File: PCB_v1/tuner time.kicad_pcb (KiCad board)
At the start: 4 copper layers, 80 x 40 mm, 118 parts, among them J1 B6B-PH-K-S, J10 1051640001, J2 B6B-PH-K-S, J3 JST_B2B-XH-A, J4 Conn_01x05_Pin, J5 Conn_01x05_Pin, J6 OLED Conn_02x04, J7 B4B-XH-A, J8 Conn_ARM_JTAG_SWD_10, J9 Conn_01x03, SW1 SW_SPST, SW2 SW_Push, SW3 SW_Push, SW4 SW_Push, SW5 SW_Push, SW6 SW_Push, SW7 SW_Push, SW8 SW_Push, SW9 SW_SPDT, U1 BQ25185DLHR, U2 BQ27441-G1, U3 SMS05T1G, U4 SMS05T1G, U5 DRV8834PWP, U6 STM32F405RGTx, U7 ESD9B5.0ST5G, Y1 Crystal

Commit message: before major move
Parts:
- removed the C15 at (181.3, 114.4)
- removed the C18 at (183.7, 120.7)
- removed the C19 at (181.2, 114.2)
- removed the C20 at (181.4, 116.2)
- removed C29: 100nF, C_0805_2012Metric
- removed C30: 1uF, C_1206_3216Metric_Pad1.33x1.80mm_HandSolder
- removed FB1: FerriteBead, L_0603_1608Metric
- removed JP3: M2, SolderJumper-3_P1.3mm_Open_RoundedPad1.0x1.5mm
- removed JP4: SLP, SolderJumper-3_P1.3mm_Bridged12_RoundedPad1.0x1.5mm
- removed the R21 at (180.9, 119.9)
- removed RN4: 22, RESCAXE80P320X160X70-8N
- removed TP1, TP2: ~, TestPoint_THTPad_D1.0mm_Drill0.5mm
- removed the TP8 at (184.4, 116.2)
- removed XTAL1: MC-306 32.7680K-E3:ROHS, SO4_MC-306_SEC
- removed Y1: Crystal, LFXTAL003237Bulk
- added H3: MountingHole, MountingHole:MountingHole_2.2mm_M2_DIN965_Pad_TopOnly, F.Cu at (152.7, 137.3)
- added J9: Conn_02x05_Odd_Even, Connector_IDC:IDC-Header_2x05_P2.54mm_Vertical, F.Cu at (196.3, 104.2)
- added JP5: M1, Jumper:SolderJumper-3_P1.3mm_Open_RoundedPad1.0x1.5mm, F.Cu at (239.4, 102.0)
- added JP6: M2, Jumper:SolderJumper-3_P1.3mm_Open_RoundedPad1.0x1.5mm, F.Cu at (239.4, 105.9)
- added JP7: SLP, Jumper:SolderJumper-3_P1.3mm_Bridged12_RoundedPad1.0x1.5mm, F.Cu at (239.4, 109.7)
- added R23: 10k, Resistor_SMD:R_0805_2012Metric, F.Cu at (178.5, 117.8)
- added R24: 47k, Resistor_SMD:R_0805_2012Metric, F.Cu at (244.4, 104.7)
- added TP13: ~, Library:TestPoint_THTPad_D0.8mm_Drill0.4mm, F.Cu at (243.2, 110.3)
- added U6: MAX7375AXR805, Package_TO_SOT_SMD:SOT-323_SC-70, F.Cu at (160.4, 80.3)
- C1, C11, C12, C13, C14, C2, C3, C4, C5, C8, C9: footprint C_0805_2012Metric -> Capacitor_SMD:C_0805_2012Metric
- C15: renamed from C17; footprint C_0805_2012Metric -> Capacitor_SMD:C_0805_2012Metric
- C16: value 0.01uF -> 100nF; footprint C_0805_2012Metric -> Capacitor_SMD:C_0805_2012Metric
- C17: renamed from C21; footprint C_0805_2012Metric -> Capacitor_SMD:C_0805_2012Metric
- C18: renamed from C22; footprint C_0805_2012Metric -> Capacitor_SMD:C_0805_2012Metric
- C19: renamed from C23; footprint C_0805_2012Metric -> Capacitor_SMD:C_0805_2012Metric
- C20: renamed from C24; footprint C_0805_2012Metric -> Capacitor_SMD:C_0805_2012Metric
- C21: renamed from C25; footprint C_0805_2012Metric -> Capacitor_SMD:C_0805_2012Metric
- C22: renamed from C26; footprint C_0805_2012Metric -> Capacitor_SMD:C_0805_2012Metric
- C23: renamed from C27; footprint C_0805_2012Metric -> Capacitor_SMD:C_0805_2012Metric
- C24: renamed from C28; footprint C_0805_2012Metric -> Capacitor_SMD:C_0805_2012Metric
- C25: renamed from C31; footprint C_1206_3216Metric_Pad1.33x1.80mm_HandSolder -> Capacitor_SMD:C_1206_3216Metric_Pad1.33x1.80mm_HandSolder
- D3: footprint LED_0805_2012Metric_Pad1.15x1.40mm_HandSolder -> LED_SMD:LED_0805_2012Metric_Pad1.15x1.40mm_HandSolder
- H1, H2: footprint MountingHole_2.2mm_M2_DIN965_Pad_TopOnly -> MountingHole:MountingHole_2.2mm_M2_DIN965_Pad_TopOnly
- J10: renamed from J9; footprint PinHeader_1x03_P2.54mm_Vertical -> Connector_PinHeader_2.54mm:PinHeader_1x03_P2.54mm_Vertical
- J3: value JST_B2B-XH-A -> JST_B2B-PH-K-S; footprint JST_B2B-XH-A -> GT_library:JST_B2B-PH-K-S
- J4, J5: footprint PinHeader_1x05_P2.54mm_Vertical -> Connector_PinHeader_2.54mm:PinHeader_1x05_P2.54mm_Vertical
- J6: footprint PinHeader_2x04_P2.54mm_Vertical -> Connector_PinHeader_2.54mm:PinHeader_2x04_P2.54mm_Vertical
- J8: value Conn_ARM_JTAG_SWD_10 -> Conn_01x02_Pin; footprint PinHeader_2x05_P2.54mm_Vertical -> Connector_PinHeader_2.54mm:PinHeader_1x02_P2.54mm_Vertical
- JP1: footprint SolderJumper-2_P1.3mm_Bridged2Bar_RoundedPad1.0x1.5mm -> Jumper:SolderJumper-2_P1.3mm_Bridged2Bar_RoundedPad1.0x1.5mm
- JP2: value M1 -> SolderJumper_2_Open; footprint SolderJumper-3_P1.3mm_Open_RoundedPad1.0x1.5mm -> Jumper:SolderJumper-2_P1.3mm_Open_RoundedPad1.0x1.5mm; moved to F.Cu
- R1, R10, R11, R12, R13, R14, R15, R16, R17, R18, R19, R2, R20, R3, R4, R5, R6, R7, R8, R9: footprint R_0805_2012Metric -> Resistor_SMD:R_0805_2012Metric
- R21: renamed from R22; footprint R_0805_2012Metric -> Resistor_SMD:R_0805_2012Metric
- R22: renamed from R23; footprint R_0805_2012Metric -> Resistor_SMD:R_0805_2012Metric
- RN1, RN2: footprint RESCAXE50P280X160X55-16N -> Parts_Library:RESCAXE50P280X160X55-16N
- RN3: footprint RESCAXS80P320X160X60-8N -> Parts_Library:RESCAXS80P320X160X60-8N
- RV1: footprint TRIM_TC33X-2-103E -> Parts_Library:TRIM_TC33X-2-103E
- SW9: footprint SW_SPDT_PCM12 -> Button_Switch_SMD:SW_SPDT_PCM12
- TP10: renamed from TP11; footprint TestPoint_THTPad_D1.0mm_Drill0.5mm -> Library:TestPoint_THTPad_D0.8mm_Drill0.4mm
- TP11: renamed from TP12; footprint TestPoint_THTPad_D1.0mm_Drill0.5mm -> Library:TestPoint_THTPad_D0.8mm_Drill0.4mm
- TP12: renamed from TP13; footprint TestPoint_THTPad_D1.0mm_Drill0.5mm -> Library:TestPoint_THTPad_D0.8mm_Drill0.4mm
- TP3, TP4, TP5, TP6, TP7: footprint TestPoint_THTPad_D1.0mm_Drill0.5mm -> Library:TestPoint_THTPad_D0.8mm_Drill0.4mm
- TP8: renamed from TP9; footprint TestPoint_THTPad_D1.0mm_Drill0.5mm -> Library:TestPoint_THTPad_D0.8mm_Drill0.4mm
- TP9: renamed from TP10; footprint TestPoint_THTPad_D1.0mm_Drill0.5mm -> Library:TestPoint_THTPad_D0.8mm_Drill0.4mm
- U8: renamed from U7; footprint SODFL1006X40N -> Library:SODFL1006X40N
- moved C21 51.2 mm to (244.5, 146.7)
- moved R22 51.2 mm to (242.1, 146.7)
- moved J4 50.3 mm to (217.0, 105.1)
- moved R3 42.4 mm to (244.4, 101.7), turned to 0 degrees
- moved SW9 40.1 mm to (163.1, 74.3), turned to 0 degrees
- moved C16 39.8 mm to (164.8, 79.8), turned to 0 degrees
- moved TP7 38.8 mm to (168.1, 79.3)
- moved C14 38.7 mm to (246.7, 112.8)
- moved R20 38.7 mm to (250.2, 112.8)
- moved JP1 38.7 mm to (245.1, 113.5)
- moved D3 38.6 mm to (244.6, 107.7), turned to 0 degrees
- moved SW8 38.5 mm to (241.7, 141.1)
- moved R18 38.5 mm to (251.9, 139.2)
- moved R19 38.5 mm to (249.9, 139.2)
- moved D6 32.8 mm to (233.7, 93.7)
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- renumbered J10 to J11, U6 to U7
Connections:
- C9 pad 1: 3V3 -> VINT
- J6 pad 5: RST -> MOSI
- J6 pad 8: MOSI -> RST
- JP2 pad 2: /Motor/M1 -> Net-(JP2-B)
- R13 pad 1: 3V3 -> VINT
- R13 pad 2: Net-(U5-CONFIG) -> Net-(JP2-B)
- R17 pad 2: /Motor/SLP -> /Motor/SLEEP
- R3 pad 2: GND -> AGND
- SW9 pad 1: 3V3 -> GND
- SW9 pad 3: GND -> 3V3
- TP7 pad 1: PC14-OSC32IN -> PH1-OSCOUT
- U5 pad 1: /Motor/A1 -> /Motor/SLEEP
- U5 pad 10: /Motor/M0 -> /Motor/EN
- U5 pad 11: /Motor/M1 -> STEP
- U5 pad 12: Net-(U5-CONFIG) -> DIR
- U5 pad 13: Net-(U5-FAULT) -> /Motor/M0
- U5 pad 14: Net-(U5-VCP) -> /Motor/M1
- U5 pad 15: VMOT -> Net-(JP2-B)
- U5 pad 16: VMOT -> Net-(U5-FAULT)
- U5 pad 17: 3V3 -> Net-(U5-VCP)
- U5 pad 18: AGND -> VMOT
- U5 pad 19: /Motor/VREF -> VMOT
- U5 pad 2: Net-(U5-AISEN) -> Net-(U5-BDECAY)
- U5 pad 20: /Motor/VREF -> VINT
- U5 pad 21: Net-(U5-VREF0) -> AGND
- U5 pad 22: /Motor/SLP -> /Motor/VREF
- U5 pad 23: Net-(U5-BDECAY) -> /Motor/VREF
- U5 pad 24: Net-(U5-ADECAY) -> Net-(U5-VREF0)
- U5 pad 3: /Motor/A2 -> Net-(U5-ADECAY)
- U5 pad 4: /Motor/B2 -> /Motor/A1
- U5 pad 5: Net-(U5-BAISEN) -> Net-(U5-AISEN)
- U5 pad 6: /Motor/B1 -> /Motor/A2
- U5 pad 7: /Motor/EN -> /Motor/B2
- U5 pad 8: STEP -> Net-(U5-BAISEN)
- U5 pad 9: DIR -> /Motor/B1
- U7 pad 13: +3.3VA -> 3V3
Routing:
- net VSYS: track 58.2 -> 0.00 mm
- net I2S_WS: track 47.9 -> 0.00 mm
- net I2S_DATA: track 45.5 -> 0.00 mm
- net I2S_BCLK: track 35.3 -> 0.00 mm, vias 2 -> 0
- net STEP: track 32.5 -> 0.00 mm, vias 2 -> 0
- net NRST: track 27.7 -> 0.00 mm, vias 3 -> 0
- net DC: track 26.2 -> 0.00 mm, vias 3 -> 0
- net SWDIO: track 23.4 -> 0.00 mm, vias 2 -> 0
- net RST: track 21.7 -> 0.00 mm, vias 2 -> 0
- net Button5: track 20.8 -> 0.00 mm, vias 1 -> 0
- net CS: track 20.4 -> 0.00 mm, vias 1 -> 0
- net 3V3: track 19.9 -> 0.00 mm
- net Button6: track 19.8 -> 0.00 mm, vias 1 -> 0
- net Button4: track 19.5 -> 0.00 mm, vias 2 -> 0
- net SWCLK: track 17.9 -> 0.00 mm, vias 2 -> 0
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- added copper zone on F.Cu, net (none)

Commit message: Placement done
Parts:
- moved JP2 105.0 mm to (141.0, 153.0)
- moved TP13 105.0 mm to (144.7, 146.6)
- moved JP5 105.0 mm to (140.8, 138.4)
- moved JP6 105.0 mm to (140.8, 142.2)
- moved JP7 105.0 mm to (140.8, 146.1)
- moved TP7 96.7 mm to (243.2, 140.4)
- moved R18 93.8 mm to (158.1, 136.3)
- moved JP1 93.4 mm to (152.4, 125.6), turned to 90 degrees
- moved R19 92.1 mm to (158.1, 131.8), turned to 90 degrees
- moved SW9 84.4 mm to (220.1, 136.6)
- moved R3 84.4 mm to (161.3, 116.2), turned to 90 degrees
- moved D3 84.2 mm to (161.3, 120.0), turned to -90 degrees
- moved R24 83.0 mm to (163.6, 123.6), turned to -90 degrees
- moved H3 82.3 mm to (227.3, 102.7)
- moved R20 77.3 mm to (175.2, 131.5), turned to 90 degrees
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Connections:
- J10 pad 1: MCU_RX -> MCU_TX
- J10 pad 2: MCU_TX -> MCU_RX
- J6 pad 1: GND -> MOSI
- J6 pad 2: 3V3 -> GND
- J6 pad 4: CS -> 3V3
- J6 pad 5: MOSI -> SCK
- J6 pad 7: SCK -> CS
- R3 pad 2: AGND -> GND
- U3 pad 1: /UI/B3 -> /UI/B4
- U3 pad 3: /UI/B2 -> /UI/B3
- U3 pad 4: /UI/B1 -> /UI/B2
- U3 pad 6: /UI/B4 -> /UI/B1
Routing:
- net BATT_POS: track 22.3 -> 5.46 mm, vias 1 -> 0
- net Net-(U1-ILIM/VSET): track 13.9 -> 1.87 mm, vias 2 -> 1
- net Net-(U1-TS/MR): track 11.6 -> 1.02 mm, vias 2 -> 1
- net VBAT: track 10.2 -> 4.43 mm
- net STATS2: track 1.06 -> 4.57 mm
- net 3V3: track 0.00 -> 2.69 mm
- net GND: track 1.73 -> 4.42 mm
- net Net-(U2-BIN): track 2.29 -> 0.00 mm
- net Net-(JP2-B): track 2.18 -> 0.00 mm
- net Net-(U2-V_{DD}): track 2.09 -> 0.00 mm
- net /Motor/M1: track 1.75 -> 0.00 mm, vias 1 -> 0
- net Net-(U5-FAULT): track 0.00 -> 1.35 mm, vias 0 -> 1
- net SCL: track 1.03 -> 0.00 mm, vias 1 -> 0
- net /Motor/M0: track 0.97 -> 0.00 mm, vias 1 -> 0
- net SDA: track 0.66 -> 0.00 mm, vias 1 -> 0
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- removed copper zone on F.Cu, net (none)
- removed copper zone on F.Cu, net VMOT

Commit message: placment is done now I swear
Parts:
- moved TP11 51.1 mm to (209.6, 128.0)
- moved TP12 49.3 mm to (210.8, 128.0)
- moved TP8 40.6 mm to (196.0, 117.5)
- moved TP10 39.4 mm to (198.0, 116.5)
- moved TP7 36.7 mm to (213.3, 119.0)
- moved TP9 34.4 mm to (196.9, 117.0)
- moved R9 7.40 mm to (170.2, 112.3)
- moved SW2 3.18 mm to (173.9, 103.5)
- moved C2 2.86 mm to (163.8, 109.8), turned to 0 degrees
- moved SW3 2.65 mm to (179.4, 103.5)
- moved J9 2.21 mm to (197.6, 136.3)
- moved SW4 2.13 mm to (184.9, 103.5)
- moved R12 1.98 mm to (170.2, 105.4), turned to -90 degrees
- moved C15 1.75 mm to (221.4, 116.0)
- moved R23 1.75 mm to (221.4, 118.2)
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
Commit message: before DRC
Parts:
- removed JP2: SolderJumper_2_Open, Jumper:SolderJumper-2_P1.3mm_Open_RoundedPad1.0x1.5mm
- added TP1: ~, Library:TestPoint_THTPad_D0.8mm_Drill0.4mm, F.Cu at (178.0, 137.7)
- JP5, JP6, JP7: moved to B.Cu
- moved TP4 54.2 mm to (193.6, 107.5)
- moved TP6 53.9 mm to (192.4, 109.3)
- moved TP5 52.8 mm to (193.6, 108.8)
- moved TP3 51.0 mm to (192.4, 107.5)
- moved TP13 36.7 mm to (174.6, 125.4)
- moved JP5 35.9 mm to (176.5, 134.2)
- moved JP6 34.1 mm to (174.0, 134.1), turned to 180 degrees
- moved JP7 30.2 mm to (163.6, 126.1)
- moved C24 13.3 mm to (208.9, 109.5)
- moved U8 7.84 mm to (162.6, 106.2), turned to 180 degrees
- moved RN2 6.82 mm to (189.4, 115.7), turned to -90 degrees
- moved R9 5.21 mm to (166.3, 108.8)
- moved C7 3.19 mm to (192.8, 112.0), turned to 0 degrees
- moved U3 2.98 mm to (178.0, 108.8)
- moved C6 2.57 mm to (186.0, 112.0), turned to 0 degrees
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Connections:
- net MISO renamed SPI1_MISO
- net MOSI renamed SPI1_MOSI
- net Net-(JP2-B) renamed /Motor/Vconfig
- net SCK renamed SPI1_SCK
- net SWCLK renamed JTAG_SWCLK
- net SWDIO renamed JTAG_SWDIO
- J6 pad 7: CS -> RST
- J6 pad 8: RST -> CS
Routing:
- net STEP: track 0.00 -> 70.9 mm, vias 1 -> 4
- net DIR: track 0.00 -> 68.2 mm, vias 1 -> 4
- net I2S_WS: track 0.00 -> 59.9 mm, vias 0 -> 2
- net NRST: track 0.00 -> 55.7 mm, vias 0 -> 3
- net SDA: track 0.00 -> 53.5 mm, vias 0 -> 2
- net I2S_BCLK: track 0.00 -> 52.5 mm, vias 0 -> 1
- net SCL: track 0.00 -> 51.6 mm, vias 0 -> 2
- net BAT_EMPTY: track 0.70 -> 51.5 mm, vias 1 -> 3
- net I2S_DATA: track 0.00 -> 49.9 mm, vias 0 -> 1
- net 3V3: track 2.69 -> 40.8 mm, vias 0 -> 13
- net Button2: track 0.00 -> 37.2 mm, vias 0 -> 3
- net GND: track 4.42 -> 41.3 mm, vias 0 -> 15
- net Button1: track 0.00 -> 36.3 mm, vias 0 -> 2
- net Button3: track 0.00 -> 34.2 mm, vias 0 -> 2
- net Button5: track 0.00 -> 29.4 mm, vias 0 -> 2
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- added copper zone on In2.Cu, net 3V3
- added copper zone on B.Cu, net AGND
- added copper zone on F.Cu, net AGND
- added copper zone on In1.Cu, net AGND
- added copper zone on B.Cu, net GND
- added copper zone on In1.Cu, net GND
- added copper zone on In2.Cu, net Net-(J8-Pin_2)
- added copper zone on F.Cu, net Net-(SW1-A)
- added copper zone on F.Cu, net VMOT
- added copper zone on In2.Cu, net VMOT
- added copper zone on In2.Cu, net VSYS

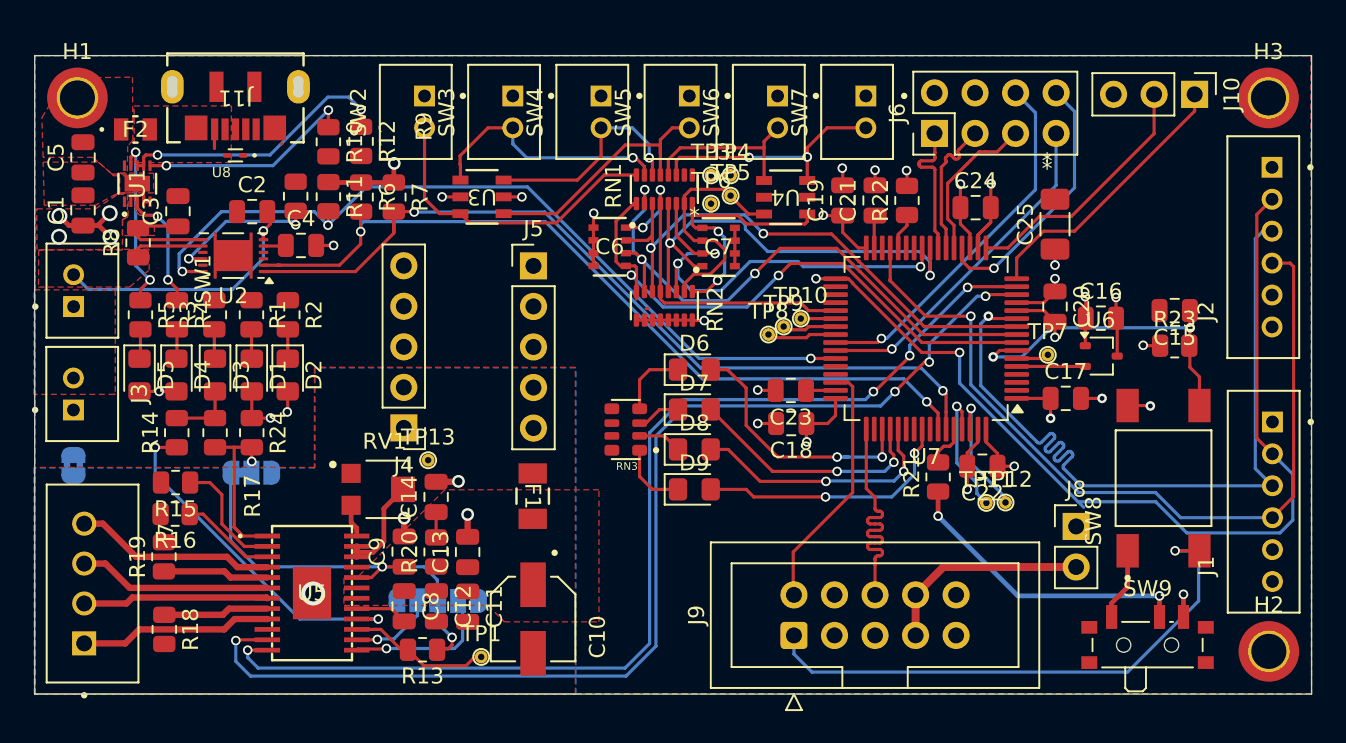
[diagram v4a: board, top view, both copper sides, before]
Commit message: done no text before stiching via
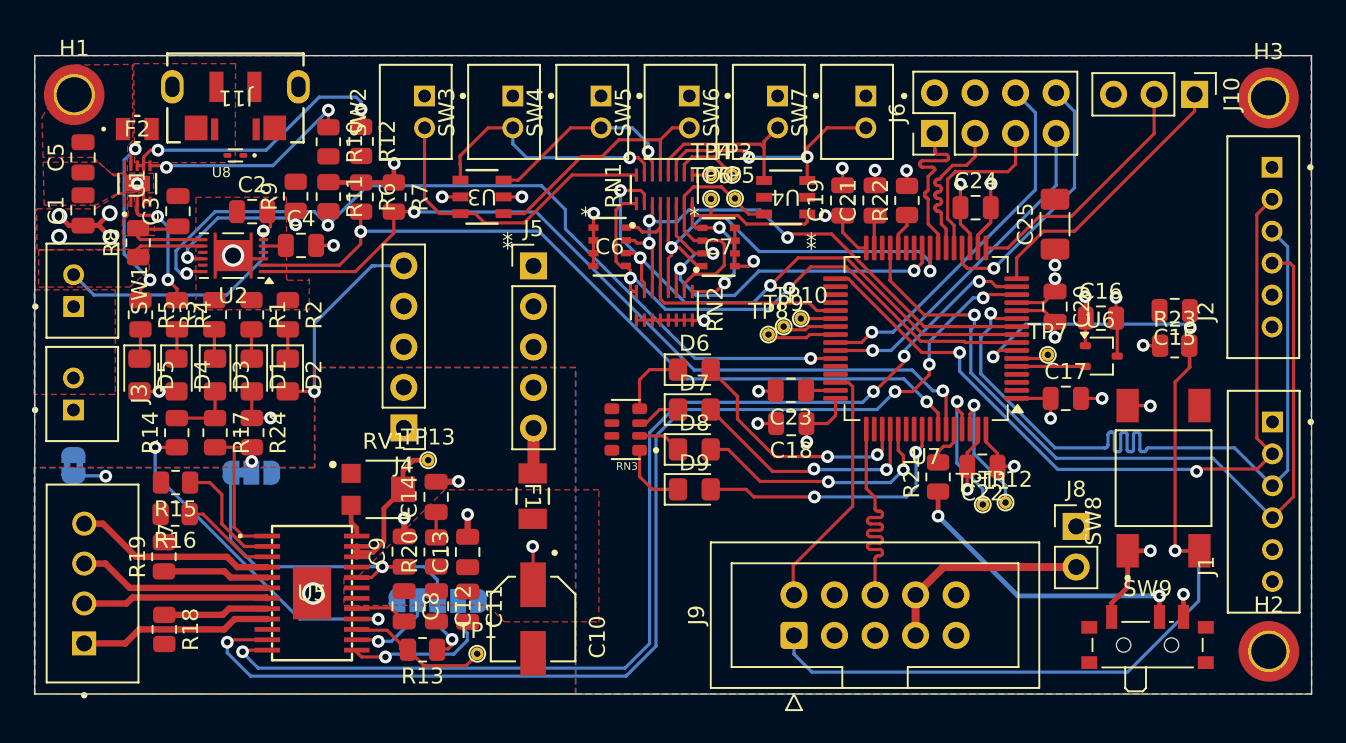
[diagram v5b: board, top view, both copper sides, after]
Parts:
- C1, C11, C12, C13, C14, C15, C16, C17, C18, C19, C2, C20, C21, C22, C23, C24, C3, C4, C5, C8, C9: footprint Capacitor_SMD:C_0805_2012Metric -> Library:C_0805_2012Metric
- C10: footprint CAP_EEE1AA101WR -> Library:CAP_EEE1AA101WR
- C6, C7: footprint CAP_CA0612_3P2X1P6_YAG -> GT_library:CAP_CA0612_3P2X1P6_YAG
- D1, D2, D4, D5, D6, D7, D8, D9: footprint LED_0805_2012Metric_Pad1.15x1.40mm_HandSolder -> LED_SMD:LED_0805_2012Metric_Pad1.15x1.40mm_HandSolder
- F1: footprint C1_BEL -> Library:C1_BEL
- F2: footprint FUS_VISHAY_MFU0805_VIS -> Library:FUS_VISHAY_MFU0805_VIS
- J1, J2: footprint JST_B6B-PH-K-S -> GT_library:JST_B6B-PH-K-S
- J11: footprint CON00906_5_MOL -> Library:CON00906_5_MOL
- J7: footprint JST_B4B-XH-A -> Library:JST_B4B-XH-A
- R1, R10, R11, R12, R13, R14, R15, R16, R17, R18, R19, R2, R20, R21, R22, R23, R24, R3, R4, R5, R6, R7, R8, R9: footprint Resistor_SMD:R_0805_2012Metric -> Library:R_0805_2012Metric
- SW1, SW2, SW3, SW4, SW5, SW6, SW7: footprint JST_B2B-PH-K-S -> GT_library:JST_B2B-PH-K-S
- SW8: footprint SW_TS04-66-65-BK-160-SMT -> Library:SW_TS04-66-65-BK-160-SMT
- U1: footprint WSON10_DLH_TEX -> Library:WSON10_DLH_TEX
- U2: footprint Texas_S-PDSO-N12 -> GT_library:Texas_S-PDSO-N12
- U3, U4: footprint SOIC_05T1G_ONS -> Library:SOIC_05T1G_ONS
- U5: footprint SOP65P640X120-25N -> Library:SOP65P640X120-25N
- U7: footprint LQFP-64_10x10mm_P0.5mm -> Library:LQFP-64_10x10mm_P0.5mm
- moved TP3 1.33 mm to (193.7, 107.5)
- moved TP4 1.23 mm to (192.4, 107.5)
- moved TP5 0.33 mm to (193.9, 109.0)
- moved TP1 0.32 mm to (177.7, 137.5)
- moved TP6 0.30 mm to (192.4, 109.0)
- moved H1 0.28 mm to (152.5, 102.5)
- moved TP11 0.25 mm to (209.4, 128.1)
- moved F2 0.12 mm to (156.4, 104.6)
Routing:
- net 3V3: track 40.8 -> 52.2 mm
- net NRST: track 55.7 -> 67.0 mm
- net I2S_WS: track 59.9 -> 50.3 mm
- net Net-(RN1G-R7.2): track 0.00 -> 4.32 mm
- net GND: track 41.3 -> 44.8 mm, vias 15 -> 19
- net /Motor/VREF: track 6.40 -> 9.42 mm
- net 5V: track 0.00 -> 2.86 mm
- net VMOT: track 2.86 -> 5.27 mm, vias 1 -> 2
- net Button4: track 22.0 -> 19.6 mm, vias 2 -> 0
- net SPI1_MOSI: track 8.97 -> 10.9 mm
- net AGND: track 4.05 -> 6.00 mm, vias 4 -> 5
- net SDA: track 53.5 -> 52.0 mm
- net SPI1_SCK: track 9.76 -> 11.0 mm
- net SCL: track 51.6 -> 50.4 mm
- net STEP: track 70.9 -> 72.1 mm
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
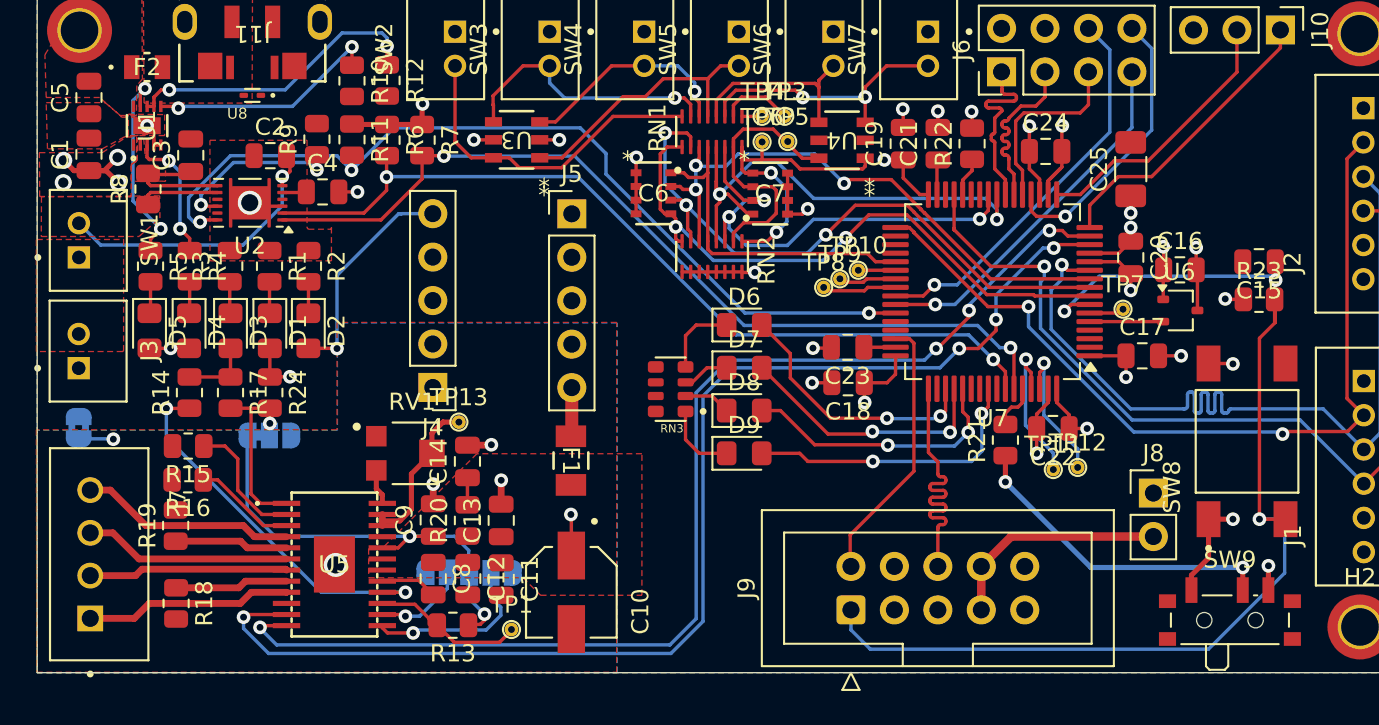
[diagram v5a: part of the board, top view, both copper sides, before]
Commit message: routing done no silkscreen
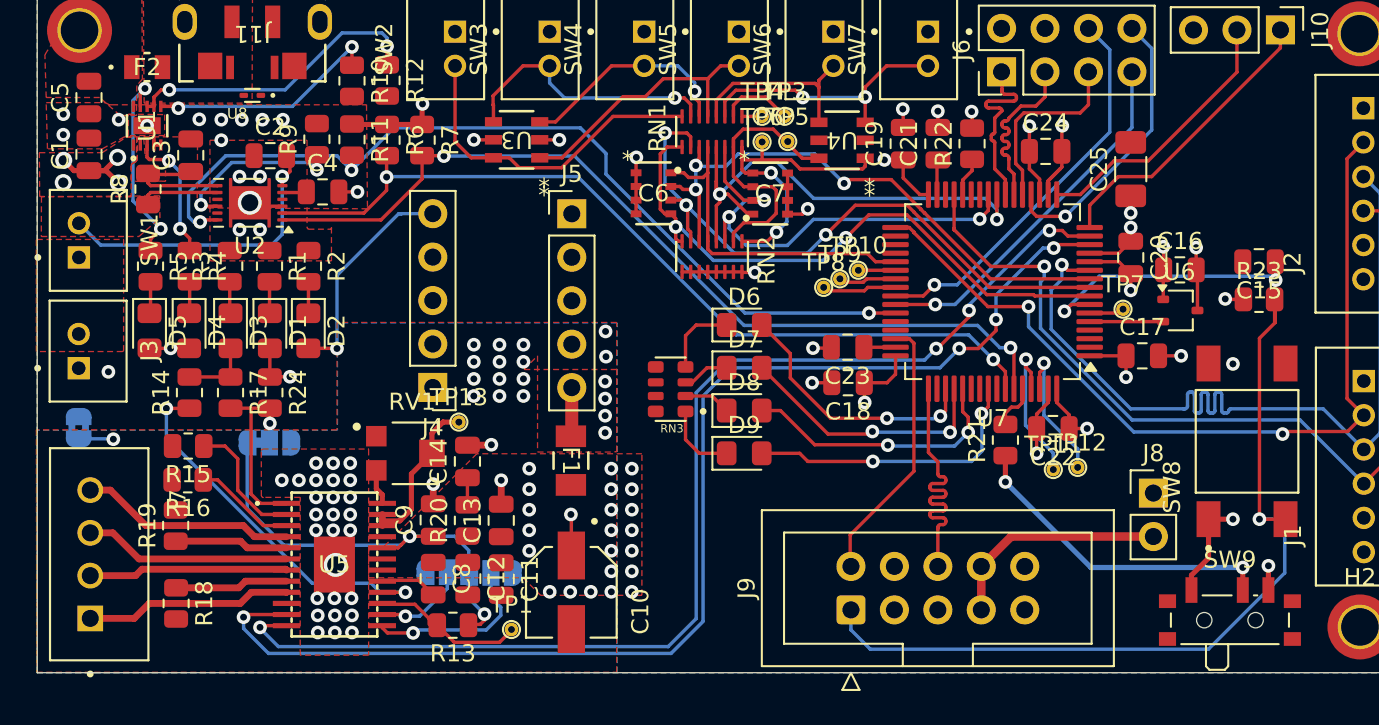
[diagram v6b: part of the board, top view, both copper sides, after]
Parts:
- moved JP7 0.42 mm to (163.6, 126.5)
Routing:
- net GND: track 44.8 -> 43.2 mm, vias 19 -> 33
- net BATT_POS: track 22.1 -> 23.1 mm
- net NRST: track 67.0 -> 66.5 mm
- net 5V: track 2.86 -> 2.79 mm, vias 0 -> 4
- net VMOT: track 5.27 -> 5.25 mm, vias 2 -> 24
- net AGND: vias 5 -> 45
- added copper zone on F.Cu, net 5V
- added copper zone on In2.Cu, net 5V
